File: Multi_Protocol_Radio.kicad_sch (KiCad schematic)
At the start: 9 parts, among them J2001 TC2050, J2002 Conn_01x06_Pin, J2003 Conn_01x06_Pin, U2001 MGM240PB32VNA3

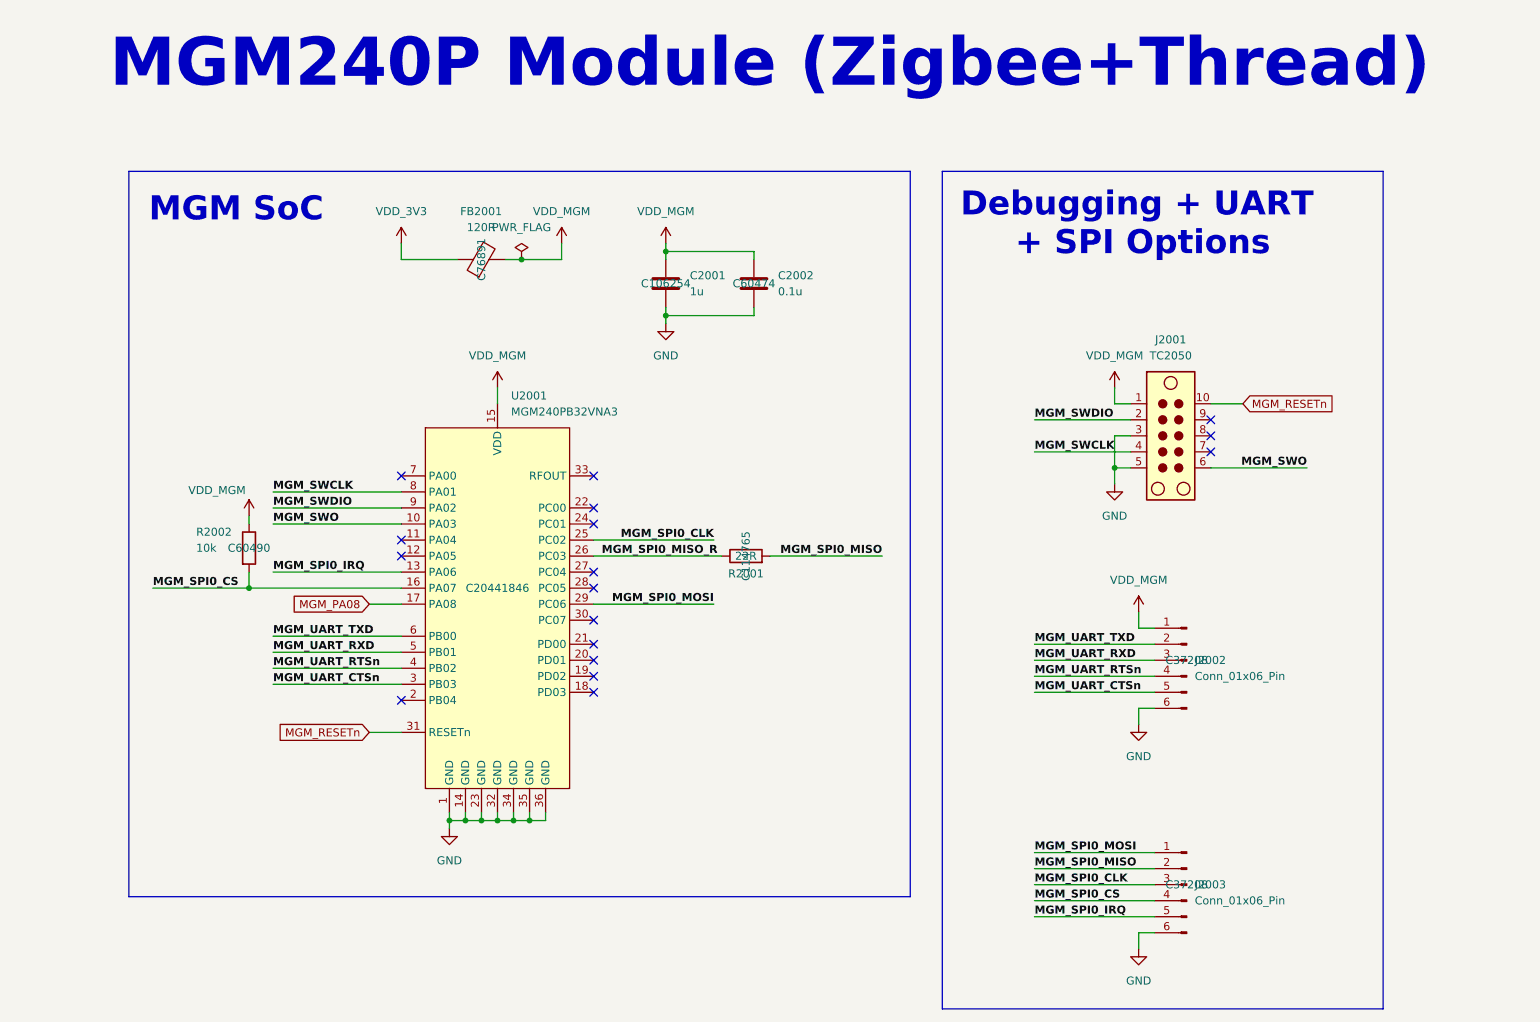
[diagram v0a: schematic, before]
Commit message: Fixed MGM240P pinout, replaced 01x06 SPI and UART header pins with 02x06 header pins that will be connected via jumper shunts, deleted MMC1 (microSD)
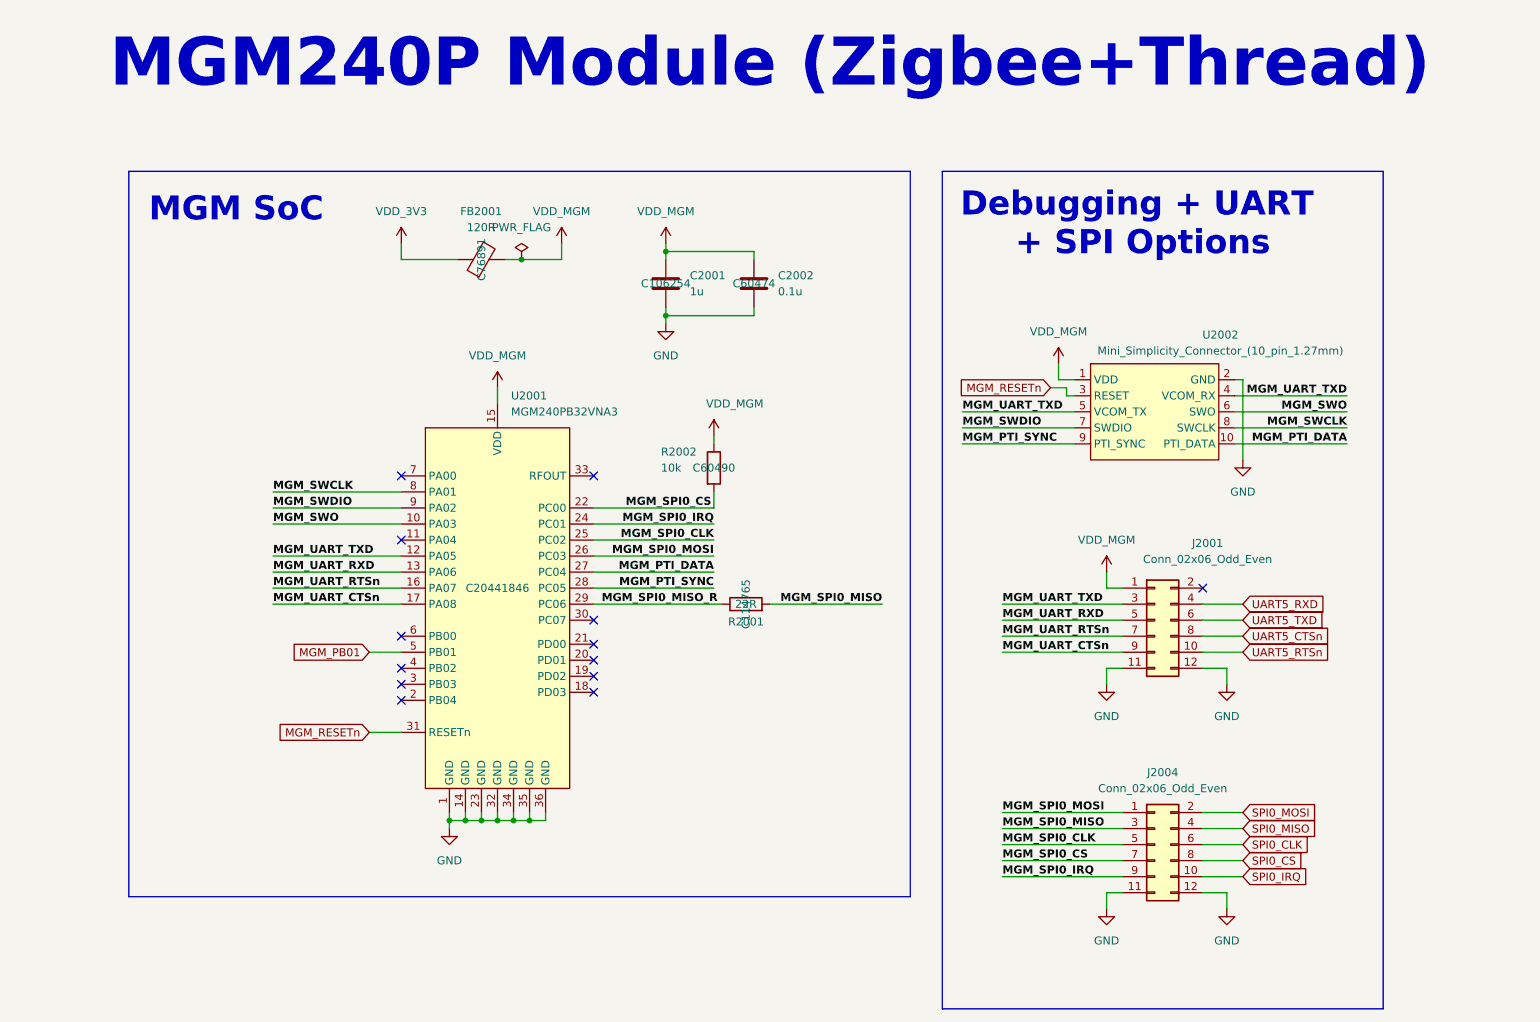
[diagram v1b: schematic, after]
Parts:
- removed J2001: TC2050, Connector:Tag-Connect_TC2050-IDC-NL_2x05_P1.27mm_Vertical, symbol Connector:TC2050
- removed J2002, J2003: Conn_01x06_Pin, Connector_PinHeader_2.54mm:PinHeader_1x06_P2.54mm_Vertical, symbol Connector:Conn_01x06_Pin
- added J2001, J2004: Conn_02x06_Odd_Even, Connector_PinHeader_2.54mm:PinHeader_2x06_P2.54mm_Vertical, symbol Connector_Generic:Conn_02x06_Odd_Even
- added U2002: Mini_Simplicity_Connector_(10_pin_1.27mm), FTSH-105-01-L-DV-K:FTSH10501LDVK, symbol SoftServicesSymbolLibrary:Mini_Simplicity_Connector_(10_pin_1.27mm)
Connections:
- net MGM_PA08 is gone; now on net MGM_UART_CTSn: U2001.17 (PA08)
- net GND: now also J2001.11 (Pin_11), J2001.12 (Pin_12), J2004.11 (Pin_11), J2004.12 (Pin_12), U2002.2 (GND)
- net MGM_RESETn: now also U2002.3 (RESET)
- net MGM_SPI0_CLK: now also J2004.5 (Pin_5)
- net MGM_SPI0_CS: now also U2001.22 (PC00), J2004.7 (Pin_7); no longer U2001.16 (PA07)
- net MGM_SPI0_IRQ: now also U2001.24 (PC01), J2004.9 (Pin_9); no longer U2001.13 (PA06)
- net MGM_SPI0_MISO: now also J2004.3 (Pin_3)
- net MGM_SPI0_MISO_R: now also U2001.29 (PC06); no longer U2001.26 (PC03)
- net MGM_SPI0_MOSI: now also U2001.26 (PC03), J2004.1 (Pin_1); no longer U2001.29 (PC06)
- net MGM_SWCLK: now also U2002.8 (SWCLK)
- net MGM_SWDIO: now also U2002.7 (SWDIO)
- net MGM_SWO: now also U2002.6 (SWO)
- net MGM_UART_CTSn: now also J2001.9 (Pin_9); no longer U2001.3 (PB03)
- net MGM_UART_RTSn: now also U2001.16 (PA07), J2001.7 (Pin_7); no longer U2001.4 (PB02)
- net MGM_UART_RXD: now also U2001.13 (PA06), J2001.5 (Pin_5); no longer U2001.5 (PB01)
- net MGM_UART_TXD: now also U2001.12 (PA05), J2001.3 (Pin_3), U2002.4 (VCOM_RX), U2002.5 (VCOM_TX); no longer U2001.6 (PB00)
- net VDD_MGM: now also J2001.1 (Pin_1), U2002.1 (VDD)
- net MGM_PTI_DATA: now reaches U2001.27 (PC04)
- net MGM_PTI_DATA: now also U2002.10 (PTI_DATA)
- net MGM_PTI_SYNC: now reaches U2001.28 (PC05)
- net MGM_PTI_SYNC: now also U2002.9 (PTI_SYNC)
- new net MGM_PB01: U2001.5 (PB01)
- new net SPI0_CLK: J2004.6 (Pin_6)
- new net SPI0_CS: J2004.8 (Pin_8)
- new net SPI0_IRQ: J2004.10 (Pin_10)
- new net SPI0_MISO: J2004.4 (Pin_4)
- new net SPI0_MOSI: J2004.2 (Pin_2)
- new net UART5_CTSn: J2001.8 (Pin_8)
- new net UART5_RTSn: J2001.10 (Pin_10)
- new net UART5_RXD: J2001.4 (Pin_4)
- new net UART5_TXD: J2001.6 (Pin_6)
- no-connect marks 17 -> 13
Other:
- moved on the sheet: R2001, R2002
